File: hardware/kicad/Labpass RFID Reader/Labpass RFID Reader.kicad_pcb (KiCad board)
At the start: 2 copper layers, 193.3 x 74.4 mm, 8 parts

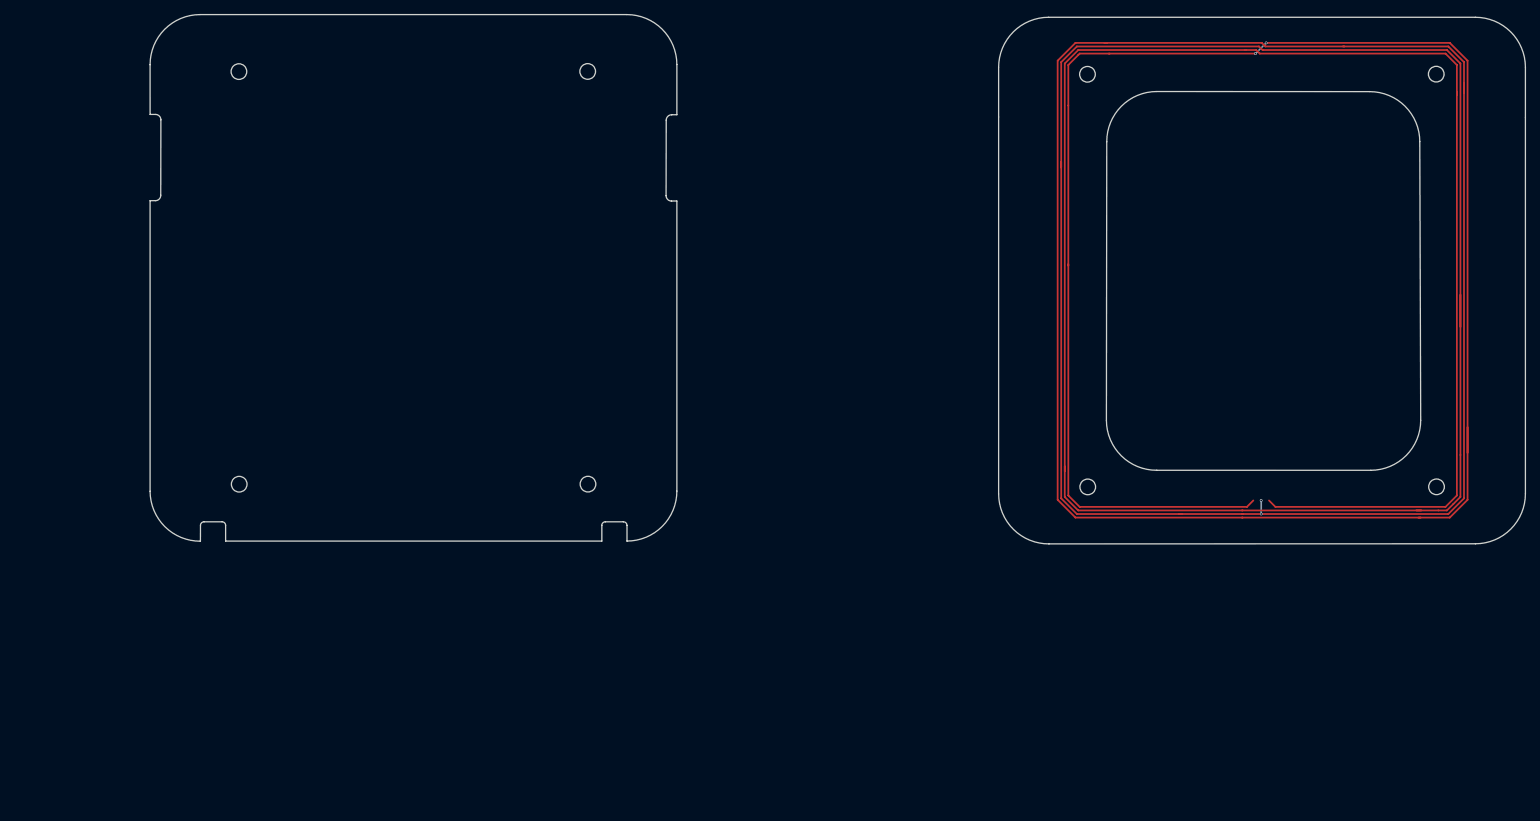
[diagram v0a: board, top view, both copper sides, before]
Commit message: Re-do board design using kicad 6.04 stable
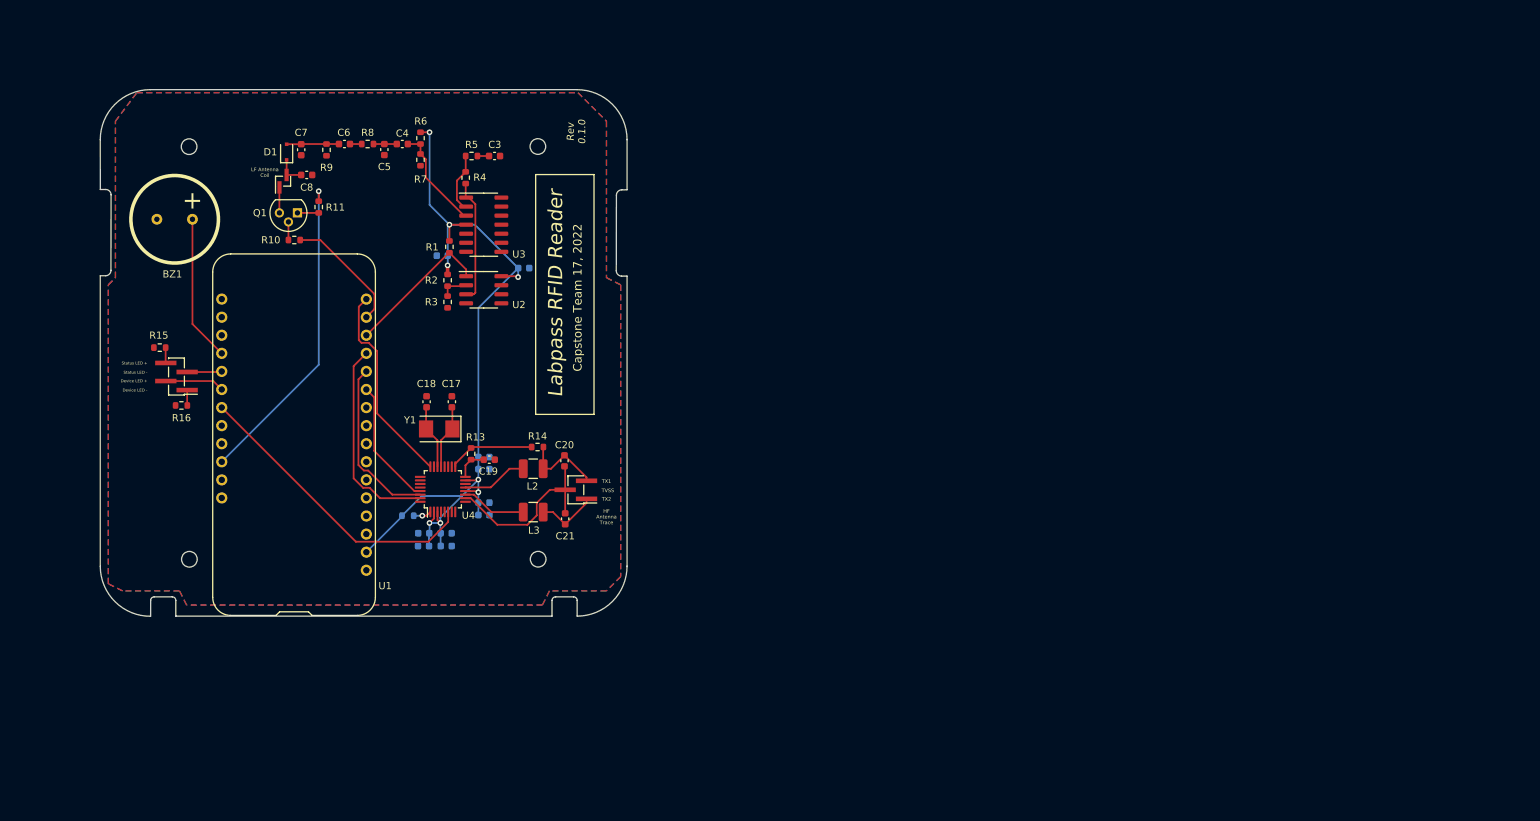
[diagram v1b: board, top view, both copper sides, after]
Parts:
- removed the REF** at (229.6, 29.4)
- removed the REF** at (229.6, 87.4)
- removed the REF** at (180.6, 87.4)
- removed the REF** at (180.6, 29.4)
- added BZ1: Buzzer, Capstone Footprint Library:buzzer, F.Cu at (52.3, 49.8)
- added C1: 1u, Capacitor_SMD:C_0603_1608Metric, B.Cu at (89.9, 54.9)
- added C10: 10u, Capacitor_SMD:C_0603_1608Metric, B.Cu at (95.8, 89.6)
- added C11: 0.1u, Capacitor_SMD:C_0603_1608Metric, B.Cu at (95.8, 84.9)
- added C12: 10u, Capacitor_SMD:C_0603_1608Metric, B.Cu at (95.8, 83.2)
- added C13: 0.1u, Capacitor_SMD:C_0603_1608Metric, B.Cu at (87.3, 95.7)
- added C14: 10u, Capacitor_SMD:C_0603_1608Metric, B.Cu at (87.3, 93.9)
- added C15: 0.1u, Capacitor_SMD:C_0603_1608Metric, B.Cu at (90.5, 95.7)
- added C16: 10u, Capacitor_SMD:C_0603_1608Metric, B.Cu at (90.5, 93.9)
- added C17: 18p, Capacitor_SMD:C_0603_1608Metric, F.Cu at (91.3, 75.4)
- added C18: 18p, Capacitor_SMD:C_0603_1608Metric, F.Cu at (87.7, 75.4)
- added C19: C, Capacitor_SMD:C_0603_1608Metric, F.Cu at (96.5, 83.6)
- added C2: 0.1u, Capacitor_SMD:C_0603_1608Metric, B.Cu at (101.4, 56.6)
- added C20: C, Capacitor_SMD:C_0603_1608Metric, F.Cu at (107.1, 83.7)
- added C21: C, Capacitor_SMD:C_0603_1608Metric, F.Cu at (107.2, 91.9)
- added C3: ~, Capacitor_SMD:C_0603_1608Metric, F.Cu at (97.3, 40.9)
- added C4: 100n, Capacitor_SMD:C_0603_1608Metric, F.Cu at (84.3, 39.2)
- added C5: 1n, Capacitor_SMD:C_0603_1608Metric, F.Cu at (81.8, 40.0)
- added C6: 22n, Capacitor_SMD:C_0603_1608Metric, F.Cu at (76.2, 39.2)
- added C7: 2.2n, Capacitor_SMD:C_0603_1608Metric, F.Cu at (70.1, 40.0)
- added C8: 10n, Capacitor_SMD:C_0603_1608Metric, F.Cu at (70.9, 43.6)
- added C9: 0.1u, Capacitor_SMD:C_0603_1608Metric, B.Cu at (95.8, 91.3)
- added D1: 1N4148, Diode_SMD:D_SOD-323F, F.Cu at (68.1, 40.3)
- added J1: Conn_01x03_Male, Connector_PinHeader_1.27mm:PinHeader_1x03_P1.27mm_Vertical_SMD_Pin1Left, F.Cu at (108.7, 87.8)
- added J2: Conn_01x04, Connector_PinHeader_1.27mm:PinHeader_1x04_P1.27mm_Vertical_SMD_Pin1Left, F.Cu at (52.6, 71.9)
- added L1: 162u, Connector_PinHeader_1.00mm:PinHeader_1x02_P1.00mm_Vertical_SMD_Pin1Left, F.Cu at (67.6, 44.4)
- added L2: L, Inductor_SMD:L_1210_3225Metric, F.Cu at (102.7, 84.8)
- added L3: L, Inductor_SMD:L_1210_3225Metric, F.Cu at (102.7, 90.9)
- added Q1: BC517, Package_TO_SOT_THT:TO-92, F.Cu at (69.6, 48.9)
- added R1: 22k, Resistor_SMD:R_0603_1608Metric, F.Cu at (90.9, 53.7)
- added R10: 1k, Resistor_SMD:R_0603_1608Metric, F.Cu at (69.1, 52.7)
- added R11: 56, Resistor_SMD:R_0603_1608Metric, F.Cu at (72.6, 48.1)
- added R12: 10k, Resistor_SMD:R_0603_1608Metric, B.Cu at (85.1, 91.4)
- added R13: R_US, Resistor_SMD:R_0603_1608Metric, F.Cu at (94.0, 82.7)
- added R14: R_US, Resistor_SMD:R_0603_1608Metric, F.Cu at (103.3, 81.8)
- added R15: R_US, Resistor_SMD:R_0603_1608Metric, F.Cu at (50.2, 67.8)
- added R16: R_US, Resistor_SMD:R_0603_1608Metric, F.Cu at (53.3, 75.9)
- added R2: 330k, Resistor_SMD:R_0603_1608Metric, F.Cu at (90.7, 58.4)
- added R3: 120k, Resistor_SMD:R_0603_1608Metric, F.Cu at (90.7, 61.4)
- added R4: 3.3k, Resistor_SMD:R_0603_1608Metric, F.Cu at (93.2, 43.9)
- added R5: 1k, Resistor_SMD:R_0603_1608Metric, F.Cu at (94.0, 40.9)
- added R6: 1M, Resistor_SMD:R_0603_1608Metric, F.Cu at (86.9, 38.4)
- added R7: 100k, Resistor_SMD:R_0603_1608Metric, F.Cu at (86.9, 41.4)
- added R8: 10k, Resistor_SMD:R_0603_1608Metric, F.Cu at (79.4, 39.2)
- added R9: 267k, Resistor_SMD:R_0603_1608Metric, F.Cu at (73.7, 40.0)
- added U1: adafruit_huzzah_32, Capstone Footprint Library:adafruit_huzzah_32, F.Cu at (69.1, 79.9)
- added U2: LM393, Package_SO:SOIC-8_3.9x4.9mm_P1.27mm, F.Cu at (95.8, 59.7)
- added U3: LM324, Package_SO:SO-14_3.9x8.65mm_P1.27mm, F.Cu at (95.8, 50.5)
- added U4: MFRC522, Package_QFP:LQFP-32_5x5mm_P0.5mm, F.Cu at (90.0, 87.7)
- added Y1: 27.12 MHz, Crystal:Crystal_SMD_5032-2Pin_5.0x3.2mm, F.Cu at (89.5, 79.2)
- moved REF** 12.7 mm to (54.4, 97.6)
- moved REF** 12.7 mm to (54.4, 39.6)
- moved REF** 12.7 mm to (103.4, 39.6)
- moved REF** 12.7 mm to (103.4, 97.6)
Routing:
- net (no net): track 966.9 -> 0.00 mm, vias 4 -> 0
- net +3V3: track 0.00 -> 120.4 mm, vias 0 -> 8
- net +5V: track 0.00 -> 45.1 mm, vias 0 -> 1
- net /labpass_rf_13.56M/RESET: track 0.00 -> 42.2 mm
- net /labpass_rf_13.56M/MISO: track 0.00 -> 28.8 mm
- net /labpass_rf_13.56M/SDA: track 0.00 -> 28.8 mm
- net /labpass_rf_13.56M/TVSS: track 0.00 -> 24.9 mm
- net /labpass_rf_13.56M/MOSI: track 0.00 -> 24.0 mm
- net /labpass_rf_125k/LF_RF_RX: track 0.00 -> 20.8 mm
- net /Indicators/buzzer: track 0.00 -> 20.5 mm
- net /labpass_rf_13.56M/SCK: track 0.00 -> 17.9 mm
- net Net-(R4-Pad2): track 0.00 -> 17.5 mm
- net /labpass_rf_125k/LF_RF_TX: track 0.00 -> 17.3 mm
- net Net-(C4-Pad1): track 0.00 -> 14.7 mm
- net /labpass_rf_13.56M/RX: track 0.00 -> 12.1 mm
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- added copper zone on B.Cu, net GND
- added copper zone on F.Cu, net GND
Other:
- board size 193.3 x 74.4 mm -> 74 x 74 mm
- board text added: "Capstone Team 17, 2022"
- board text added: "Device LED +"
- board text added: "Device LED -"
- board text added: "HF Antenna Trace"
- board text added: "LF Antenna Coil"
- board text added: "Labpass RFID Reader"
- board text added: "Rev 0.1.0"
- board text added: "Status LED +"
- board text added: "Status LED -"
- board text added: "TVSS"
- board text added: "TX1"
- board text added: "TX2"

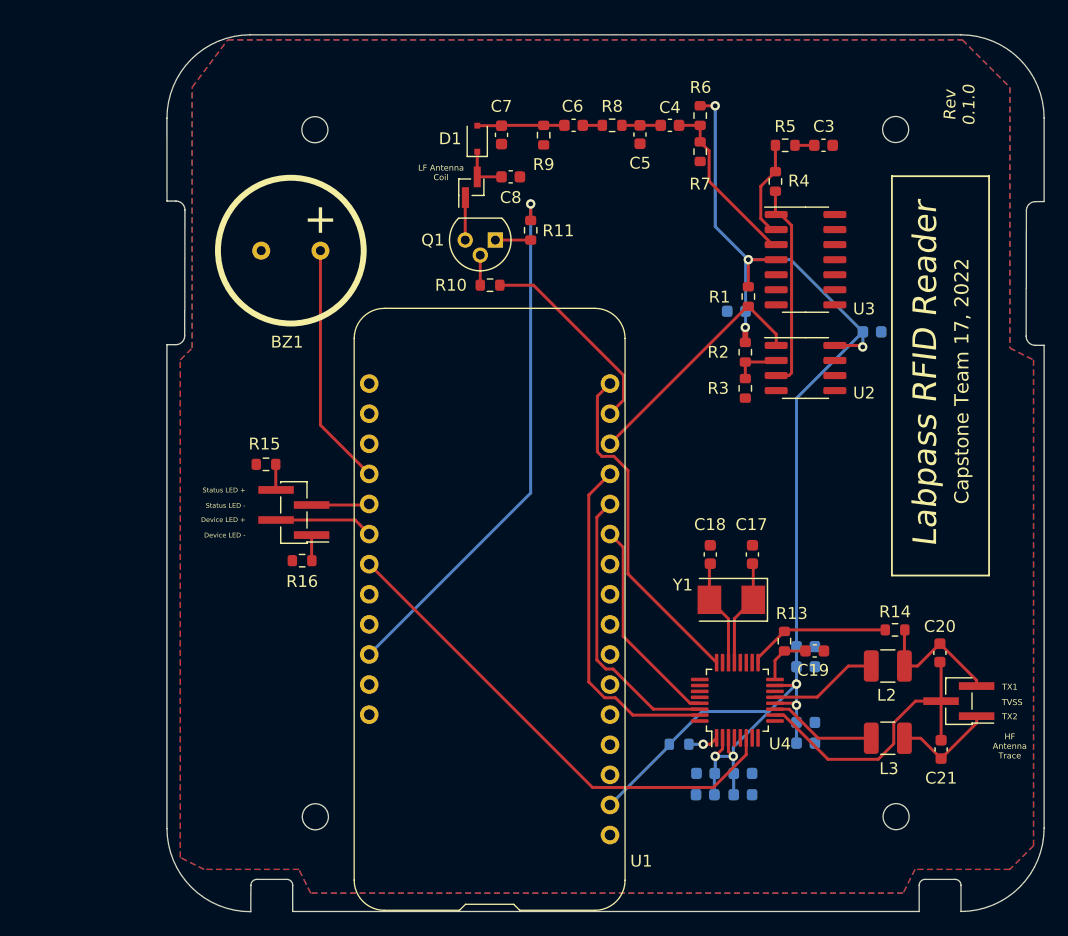
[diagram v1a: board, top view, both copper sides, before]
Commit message: Polish reposition pin headers to clear mez board
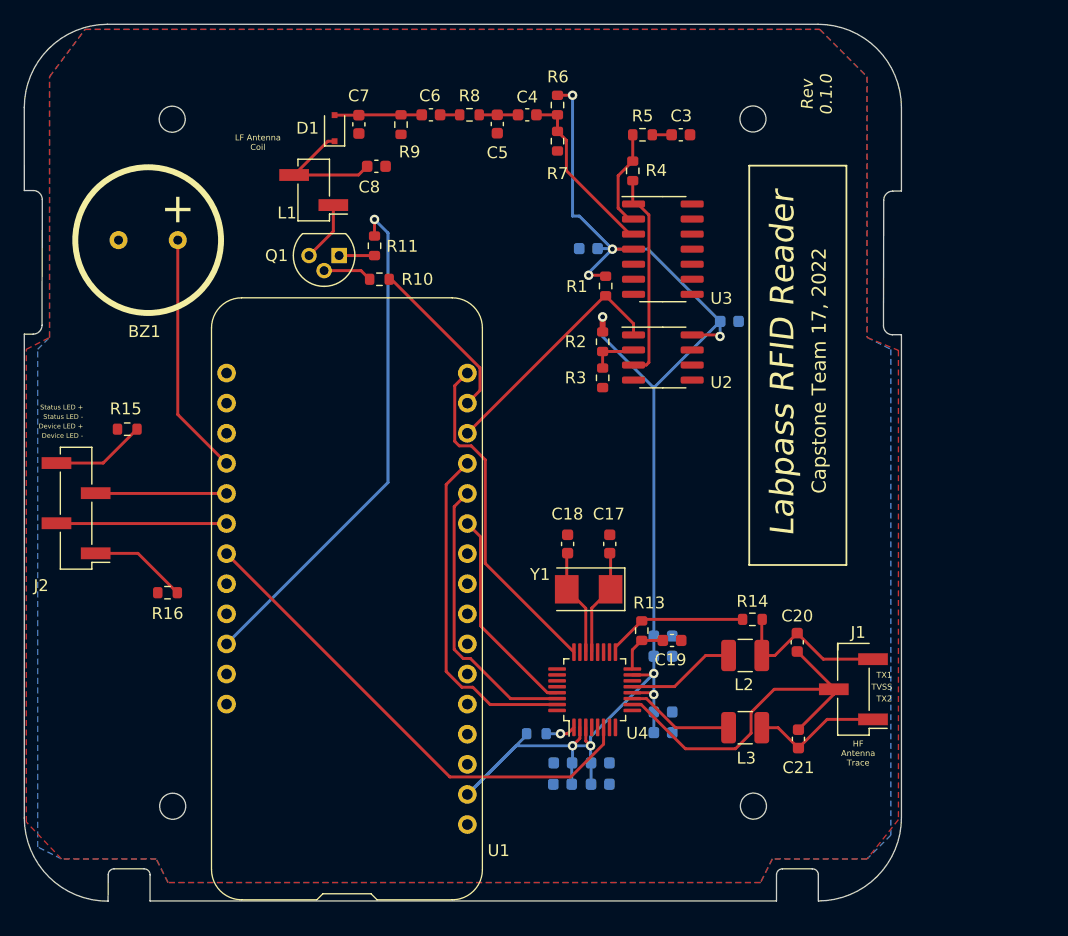
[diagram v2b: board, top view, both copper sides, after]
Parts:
- J1: footprint Connector_PinHeader_1.27mm:PinHeader_1x03_P1.27mm_Vertical_SMD_Pin1Left -> Connector_PinHeader_2.54mm:PinHeader_1x03_P2.54mm_Vertical_SMD_Pin1Left
- J2: footprint Connector_PinHeader_1.27mm:PinHeader_1x04_P1.27mm_Vertical_SMD_Pin1Left -> Connector_PinHeader_2.54mm:PinHeader_1x04_P2.54mm_Vertical_SMD_Pin1Left
- L1: footprint Connector_PinHeader_1.00mm:PinHeader_1x02_P1.00mm_Vertical_SMD_Pin1Left -> Connector_PinHeader_2.54mm:PinHeader_1x02_P2.54mm_Vertical_SMD_Pin1Left
- moved J2 18.4 mm to (34.2, 71.5)
- moved C1 13.6 mm to (77.4, 49.6)
- moved L1 13.3 mm to (54.3, 44.7), turned to 180 degrees
- moved Q1 13.2 mm to (56.4, 50.2)
- moved R11 13.2 mm to (59.4, 49.4)
- moved R15 12.1 mm to (38.5, 64.8)
- moved C10 12.1 mm to (83.7, 88.7)
- moved C11 12.1 mm to (83.7, 84.0)
- moved C12 12.1 mm to (83.7, 82.3)
- moved C13 12.1 mm to (75.3, 94.8)
- moved C14 12.1 mm to (75.3, 93.0)
- moved C17 12.1 mm to (79.2, 74.5)
- moved C18 12.1 mm to (75.7, 74.5)
- moved C19 12.1 mm to (84.5, 82.7)
- moved C2 12.1 mm to (89.3, 55.8)
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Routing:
- net Net-(C8-Pad1): track 4.16 -> 11.1 mm
- net /Indicators/status_led: track 4.90 -> 11.1 mm
- net Net-(R16-Pad1): track 2.17 -> 8.26 mm
- net /Indicators/device_led: track 8.35 -> 14.4 mm
- net /labpass_rf_13.56M/TVSS: track 24.9 -> 30.8 mm
- net +3V3: track 120.4 -> 126.3 mm, vias 8 -> 9
- net Net-(R15-Pad1): track 2.17 -> 7.98 mm
- net /labpass_rf_125k/LF_RF_TX: track 17.3 -> 14.2 mm
- net Net-(C21-Pad1): track 8.63 -> 11.1 mm
- net Net-(C20-Pad2): track 11.7 -> 14.1 mm
- net +5V: track 45.1 -> 43.3 mm
- net Net-(Q1-Pad2): track 2.54 -> 4.15 mm
- net Net-(L1-Pad1): track 3.57 -> 5.11 mm
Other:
- board text added: "mezannine board outline"
